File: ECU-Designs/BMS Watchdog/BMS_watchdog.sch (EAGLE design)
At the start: 4 parts, among them X1 MINIFIT_5566-4

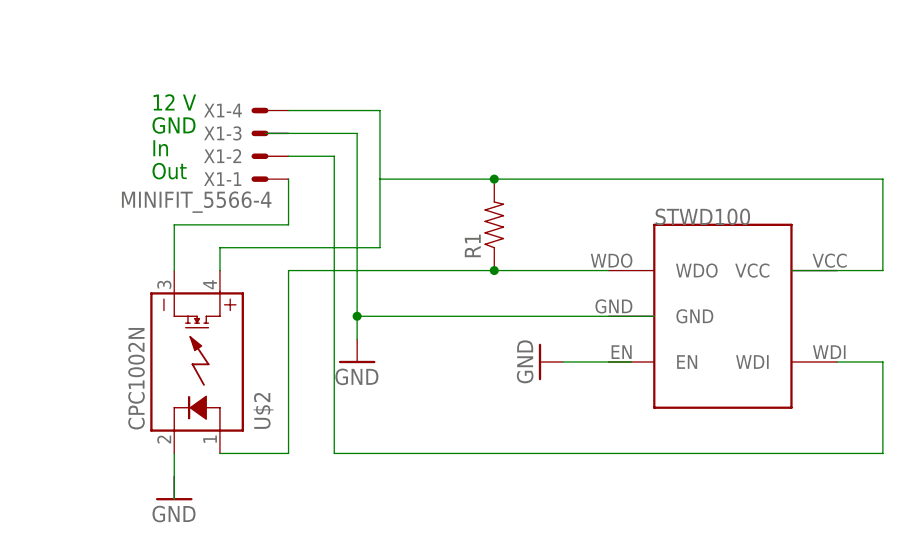
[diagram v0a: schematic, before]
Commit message: Updated BMS watchdog
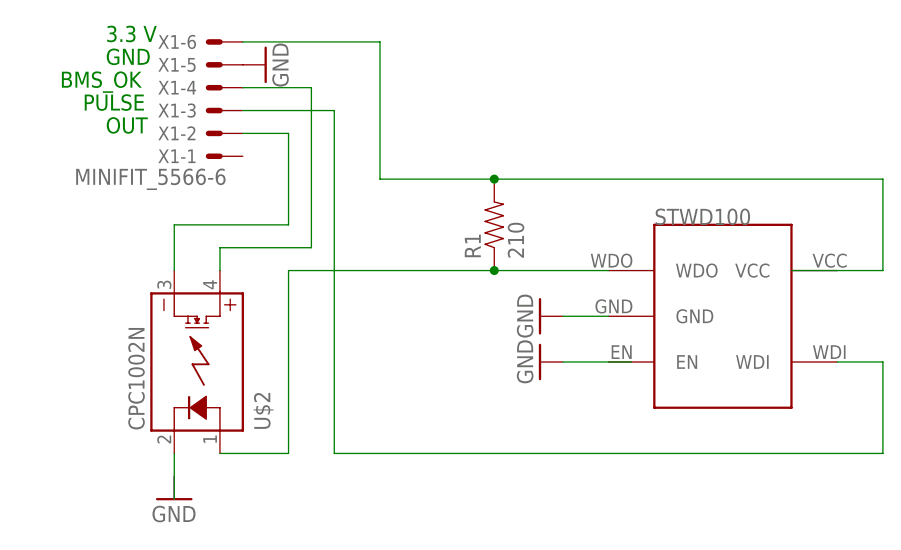
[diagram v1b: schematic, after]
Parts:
- R1: value (none) -> 210
- X1: value MINIFIT_5566-4 -> MINIFIT_5566-6; device HyTechDevices:MINIFIT_5566-4 -> HyTechDevices:MINIFIT_5566-6
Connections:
- new net GND: U$1.GND, X1-5.S
- new net N$4: U$2.DC+, X1-4.S
- net N$1: now also X1-6.S; no longer U$2.DC+, X1-4.S
- net N$2: now also X1-3.S; no longer X1-2.S
- net N$5: now also X1-2.S; no longer X1-1.S
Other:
- note added: "3.3 V"
- note added: "BMS_OK"
- note added: "OUT"
- note added: "PULSE"
- note removed: "12 V"
- note removed: "In"
- note removed: "Out"
- moved on the sheet: X1-1, X1-2, X1-3, X1-4
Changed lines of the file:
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@@
 <parts>
 <part name="U$1" library="HyTechDevices" deviceset="STWD100" device=""/>
-<part name="R1" library="HyTechDevices" deviceset="RESISTOR" device="0805-RES"/>
+<part name="R1" library="HyTechDevices" deviceset="RESISTOR" device="0805-RES" value="210"/>
 <part name="GND3" library="HyTechSymbols" deviceset="GND" device=""/>
-<part name="X1" library="HyTechDevices" deviceset="MINIFIT_5566-4" device=""/>
 <part name="U$2" library="HyTechDevices" deviceset="CPC1002N" device=""/>
 <part name="GND1" library="HyTechSymbols" deviceset="GND" device=""/>
 <part name="GND2" library="HyTechSymbols" deviceset="GND" device=""/>
+<part name="X1" library="HyTechDevices" deviceset="MINIFIT_5566-6" device=""/>
+<part name="GND4" library="HyTechSymbols" deviceset="GND" device=""/>
 </parts>
 <sheets>
 <sheet>
 <plain>
-<text x="20.32" y="83.82" size="1.778" layer="91">12 V</text>
-<text x="20.32" y="81.28" size="1.778" layer="91">GND</text>
-<text x="20.32" y="76.2" size="1.778" layer="91">Out</text>
-<text x="20.32" y="78.74" size="1.778" layer="91">In</text>
+<text x="15.24" y="91.44" size="1.778" layer="91">3.3 V</text>
+<text x="15.24" y="88.9" size="1.778" layer="91">GND</text>
+<text x="12.7" y="83.82" size="1.778" layer="91">PULSE</text>
+<text x="10.16" y="86.36" size="1.778" layer="91">BMS_OK</text>
+<text x="15.24" y="81.28" size="1.778" layer="91">OUT</text>
 </plain>
 <instances>
@@
 <instance part="R1" gate="G$1" x="58.42" y="71.12" rot="R90"/>
 <instance part="GND3" gate="1" x="63.5" y="55.88" rot="R270"/>
-<instance part="X1" gate="-1" x="33.02" y="76.2" rot="R180"/>
-<instance part="X1" gate="-2" x="33.02" y="78.74" rot="R180"/>
-<instance part="X1" gate="-3" x="33.02" y="81.28" rot="R180"/>
-<instance part="X1" gate="-4" x="33.02" y="83.82" rot="R180"/>
 <instance part="U$2" gate="G$1" x="25.4" y="55.88" rot="MR90"/>
 <instance part="GND1" gate="1" x="22.86" y="40.64"/>
-<instance part="GND2" gate="1" x="43.18" y="55.88"/>
+<instance part="GND2" gate="1" x="63.5" y="60.96" rot="R270"/>
+<instance part="X1" gate="-1" x="27.94" y="78.74" rot="R180"/>
+<instance part="X1" gate="-2" x="27.94" y="81.28" rot="R180"/>
+<instance part="X1" gate="-3" x="27.94" y="83.82" rot="R180"/>
+<instance part="X1" gate="-4" x="27.94" y="86.36" rot="R180"/>
+<instance part="X1" gate="-5" x="27.94" y="88.9" rot="R180"/>
+<instance part="X1" gate="-6" x="27.94" y="91.44" rot="R180"/>
+<instance part="GND4" gate="1" x="33.02" y="88.9" rot="R90"/>
 </instances>
 <busses>
@@
 </segment>
 <segment>
-<wire x1="33.02" y1="81.28" x2="43.18" y2="81.28" width="0.1524" layer="91"/>
-<wire x1="43.18" y1="81.28" x2="43.18" y2="60.96" width="0.1524" layer="91"/>
-<wire x1="43.18" y1="60.96" x2="76.2" y2="60.96" width="0.1524" layer="91"/>
+<pinref part="X1" gate="-5" pin="S"/>
+<pinref part="GND4" gate="1" pin="GND"/>
+</segment>
+<segment>
 <pinref part="GND2" gate="1" pin="GND"/>
-<wire x1="43.18" y1="60.96" x2="43.18" y2="58.42" width="0.1524" layer="91"/>
-<junction x="43.18" y="60.96"/>
+<pinref part="U$1" gate="G$1" pin="GND"/>
+<wire x1="66.04" y1="60.96" x2="71.12" y2="60.96" width="0.1524" layer="91"/>
 </segment>
 </net>
@@
 <wire x1="101.6" y1="55.88" x2="101.6" y2="45.72" width="0.1524" layer="91"/>
 <wire x1="101.6" y1="45.72" x2="40.64" y2="45.72" width="0.1524" layer="91"/>
-<pinref part="X1" gate="-2" pin="S"/>
-<wire x1="35.56" y1="78.74" x2="40.64" y2="78.74" width="0.1524" layer="91"/>
-<wire x1="40.64" y1="78.74" x2="40.64" y2="45.72" width="0.1524" layer="91"/>
+<wire x1="40.64" y1="83.82" x2="40.64" y2="45.72" width="0.1524" layer="91"/>
+<pinref part="X1" gate="-3" pin="S"/>
+<wire x1="40.64" y1="83.82" x2="30.48" y2="83.82" width="0.1524" layer="91"/>
 </segment>
 </net>
 <net name="N$1" class="0">
 <segment>
-<pinref part="X1" gate="-4" pin="S"/>
-<wire x1="35.56" y1="83.82" x2="45.72" y2="83.82" width="0.1524" layer="91"/>
-<wire x1="45.72" y1="83.82" x2="45.72" y2="76.2" width="0.1524" layer="91"/>
 <pinref part="R1" gate="G$1" pin="2"/>
 <wire x1="101.6" y1="76.2" x2="101.6" y2="66.04" width="0.1524" layer="91"/>
@@
 <junction x="58.42" y="76.2"/>
 <wire x1="45.72" y1="76.2" x2="58.42" y2="76.2" width="0.1524" layer="91"/>
-<wire x1="45.72" y1="76.2" x2="45.72" y2="68.58" width="0.1524" layer="91"/>
-<wire x1="45.72" y1="68.58" x2="27.94" y2="68.58" width="0.1524" layer="91"/>
-<pinref part="U$2" gate="G$1" pin="DC+"/>
-<wire x1="27.94" y1="68.58" x2="27.94" y2="66.04" width="0.1524" layer="91"/>
+<wire x1="45.72" y1="76.2" x2="45.72" y2="91.44" width="0.1524" layer="91"/>
+<pinref part="X1" gate="-6" pin="S"/>
+<wire x1="45.72" y1="91.44" x2="30.48" y2="91.44" width="0.1524" layer="91"/>
 </segment>
 </net>
@@
 <pinref part="U$2" gate="G$1" pin="DC-"/>
 <wire x1="22.86" y1="66.04" x2="22.86" y2="71.12" width="0.1524" layer="91"/>
-<pinref part="X1" gate="-1" pin="S"/>
 <wire x1="22.86" y1="71.12" x2="35.56" y2="71.12" width="0.1524" layer="91"/>
-<wire x1="35.56" y1="71.12" x2="35.56" y2="76.2" width="0.1524" layer="91"/>
+<wire x1="35.56" y1="71.12" x2="35.56" y2="81.28" width="0.1524" layer="91"/>
+<pinref part="X1" gate="-2" pin="S"/>
+<wire x1="35.56" y1="81.28" x2="30.48" y2="81.28" width="0.1524" layer="91"/>
 </segment>
 </net>
@@
 </segment>
 </net>
+<net name="N$4" class="0">
+<segment>
+<pinref part="U$2" gate="G$1" pin="DC+"/>
+<wire x1="27.94" y1="68.58" x2="27.94" y2="66.04" width="0.1524" layer="91"/>
+<wire x1="27.94" y1="68.58" x2="38.1" y2="68.58" width="0.1524" layer="91"/>
+<wire x1="38.1" y1="68.58" x2="38.1" y2="86.36" width="0.1524" layer="91"/>
+<pinref part="X1" gate="-4" pin="S"/>
+<wire x1="38.1" y1="86.36" x2="30.48" y2="86.36" width="0.1524" layer="91"/>
+</segment>
+</net>
